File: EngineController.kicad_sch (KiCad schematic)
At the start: 37 parts, among them J1 RBUS, U1 ESP32-S3, Y1 R940000171

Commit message: Finished schematic
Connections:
- net BUCK_EN: no longer U1.43 (GPIO38)
- net CAN_RX: now also U1.6 (GPIO1/ADC1_CH0); no longer U1.39 (GPIO34)
- net CAN_TX: now also U1.7 (GPIO2/ADC1_CH1); no longer U1.38 (GPIO33)
- net Servo1PWM: now also U1.16 (GPIO11/ADC2_CH0); no longer U1.41 (GPIO36)
- net Servo2PWM: now also U1.15 (GPIO10/ADC1_CH9); no longer U1.42 (GPIO37)
- net ServoV_LOG: now also U1.17 (GPIO12/ADC2_CH1); no longer U1.40 (GPIO35)
- net GPIO5: now reaches U1.10 (GPIO5/ADC1_CH4)
- net GPIO3: now reaches U1.11 (GPIO6/ADC1_CH5)
- net GPIO1: now reaches U1.12 (GPIO7/ADC1_CH6)
- net GPIO2: now reaches U1.13 (GPIO8/ADC1_CH7)
- net GPIO0: now reaches U1.14 (GPIO9/ADC1_CH8)
- net GPIO4: now reaches U1.9 (GPIO4/ADC1_CH3)
- new net AIN0N: U1.42 (GPIO37)
- new net AIN0P: U1.43 (GPIO38)
- new net AIN1N: U1.41 (GPIO36)
- new net AIN1P: U1.40 (GPIO35)
- new net AIN2N: U1.38 (GPIO33)
- new net AIN2P: U1.39 (GPIO34)
- no-connect marks 30 -> 19
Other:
- added sheet Pyro (Pyro.kicad_sch)
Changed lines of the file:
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@@
   (no_connect (at 135.89 82.55))
   (no_connect (at 135.89 115.57))
-  (no_connect (at 69.85 95.25))
-  (no_connect (at 69.85 80.01))
-  (no_connect (at 69.85 72.39))
   (no_connect (at 135.89 80.01))
   (no_connect (at 135.89 130.81))
-  (no_connect (at 69.85 85.09))
   (no_connect (at 69.85 118.11))
   (no_connect (at 69.85 77.47))
-  (no_connect (at 69.85 82.55))
   (no_connect (at 135.89 85.09))
-  (no_connect (at 69.85 92.71))
   (no_connect (at 135.89 128.27))
   (no_connect (at 69.85 62.23))
   (no_connect (at 135.89 113.03))
-  (no_connect (at 69.85 97.79))
-  (no_connect (at 69.85 87.63))
   (no_connect (at 135.89 87.63))
   (no_connect (at 135.89 92.71))
@@
   (no_connect (at 135.89 77.47))
   (no_connect (at 135.89 123.19))
-  (no_connect (at 69.85 74.93))
   (no_connect (at 69.85 123.19))
-  (no_connect (at 69.85 90.17))
   (no_connect (at 69.85 125.73))
-  (no_connect (at 69.85 100.33))
   (no_connect (at 135.89 110.49))
   (wire (pts (xy 120.65 25.4) (xy 120.65 35.56))
@@
     (stroke (width 0) (type default))
   )
-  (wire (pts (xy 139.7 97.79) (xy 135.89 97.79))
-    (stroke (width 0) (type default))
-  )
   (wire (pts (xy 45.72 165.1) (xy 53.34 165.1))
     (stroke (width 0) (type default))
@@
     (stroke (width 0) (type default))
   )
+  (wire (pts (xy 207.264 127) (xy 214.884 127))
+    (stroke (width 0) (type default))
+  )
   (polyline (pts (xy 12.7 12.7) (xy 175.26 12.7))
     (stroke (width 0) (type default))
@@
     (stroke (width 0) (type default))
   )
+  (wire (pts (xy 205.994 123.19) (xy 214.884 123.19))
+    (stroke (width 0) (type default))
+  )
   (wire (pts (xy 58.42 21.59) (xy 58.42 26.67))
     (stroke (width 0) (type default))
@@
     (stroke (width 0) (type default))
   )
-  (wire (pts (xy 139.7 95.25) (xy 135.89 95.25))
-    (stroke (width 0) (type default))
-  )
   (wire (pts (xy 58.42 26.67) (xy 58.42 40.64))
     (stroke (width 0) (type default))
@@
   )
   (wire (pts (xy 167.64 127) (xy 167.64 132.08))
+    (stroke (width 0) (type default))
+  )
+  (wire (pts (xy 207.264 130.556) (xy 214.884 130.556))
     (stroke (width 0) (type default))
   )
@@
     (effects (font (size 1.27 1.27)) (justify right bottom))
   )
+  (label "Nuke 1" (at 207.264 127 0) (fields_autoplaced)
+    (effects (font (size 1.27 1.27)) (justify left bottom))
+  )
   (label "MOSI" (at 220.98 81.28 0) (fields_autoplaced)
     (effects (font (size 1.27 1.27)) (justify left bottom))
   )
-  (label "Servo1PWM" (at 135.89 102.87 0) (fields_autoplaced)
-    (effects (font (size 1.27 1.27)) (justify left bottom))
-  )
   (label "CHIP_PU" (at 36.83 165.1 180) (fields_autoplaced)
     (effects (font (size 1.27 1.27)) (justify right bottom))
@@
     (effects (font (size 1.27 1.27)) (justify left bottom))
   )
+  (label "AIN0P" (at 135.89 107.95 0) (fields_autoplaced)
+    (effects (font (size 1.27 1.27)) (justify left bottom))
+  )
   (label "MISO" (at 220.98 83.82 0) (fields_autoplaced)
     (effects (font (size 1.27 1.27)) (justify left bottom))
@@
     (effects (font (size 1.27 1.27)) (justify left bottom))
   )
+  (label "Servo2PWM" (at 69.85 95.25 180) (fields_autoplaced)
+    (effects (font (size 1.27 1.27)) (justify right bottom))
+  )
   (label "CAN+" (at 115.57 185.42 0) (fields_autoplaced)
     (effects (font (size 1.27 1.27)) (justify left bottom))
@@
     (effects (font (size 1.27 1.27)) (justify left bottom))
   )
+  (label "Servo1PWM" (at 69.85 97.79 180) (fields_autoplaced)
+    (effects (font (size 1.27 1.27)) (justify right bottom))
+  )
   (label "Data+" (at 99.06 160.02 0) (fields_autoplaced)
     (effects (font (size 1.27 1.27)) (justify left bottom))
@@
     (effects (font (size 1.27 1.27)) (justify left bottom))
   )
+  (label "GPIO1" (at 69.85 87.63 180) (fields_autoplaced)
+    (effects (font (size 1.27 1.27)) (justify right bottom))
+  )
   (label "MOSI" (at 66.04 105.41 180) (fields_autoplaced)
     (effects (font (size 1.27 1.27)) (justify right bottom))
   )
-  (label "CAN_TX" (at 139.7 95.25 0) (fields_autoplaced)
-    (effects (font (size 1.27 1.27)) (justify left bottom))
+  (label "GPIO0" (at 69.85 92.71 180) (fields_autoplaced)
+    (effects (font (size 1.27 1.27)) (justify right bottom))
+  )
+  (label "AIN2N" (at 135.89 95.25 0) (fields_autoplaced)
+    (effects (font (size 1.27 1.27)) (justify left bottom))
+  )
+  (label "CAN_TX" (at 69.85 74.93 180) (fields_autoplaced)
+    (effects (font (size 1.27 1.27)) (justify right bottom))
   )
   (label "SCLK" (at 144.78 72.39 0) (fields_autoplaced)
@@
     (effects (font (size 1.27 1.27)) (justify left bottom))
   )
+  (label "Cont 1" (at 207.264 130.556 0) (fields_autoplaced)
+    (effects (font (size 1.27 1.27)) (justify left bottom))
+  )
   (label "Data-" (at 99.06 162.56 0) (fields_autoplaced)
     (effects (font (size 1.27 1.27)) (justify left bottom))
@@
     (effects (font (size 1.27 1.27)) (justify left bottom))
   )
+  (label "GPIO2" (at 69.85 90.17 180) (fields_autoplaced)
+    (effects (font (size 1.27 1.27)) (justify right bottom))
+  )
+  (label "AIN2P" (at 135.89 97.79 0) (fields_autoplaced)
+    (effects (font (size 1.27 1.27)) (justify left bottom))
+  )
   (label "BOOT" (at 68.58 165.1 180) (fields_autoplaced)
     (effects (font (size 1.27 1.27)) (justify right bottom))
   )
-  (label "ServoV_LOG" (at 135.89 100.33 0) (fields_autoplaced)
-    (effects (font (size 1.27 1.27)) (justify left bottom))
-  )
-  (label "CAN_RX" (at 139.7 97.79 0) (fields_autoplaced)
+  (label "ServoV_LOG" (at 69.85 100.33 180) (fields_autoplaced)
+    (effects (font (size 1.27 1.27)) (justify right bottom))
+  )
+  (label "GPIO5" (at 69.85 82.55 180) (fields_autoplaced)
+    (effects (font (size 1.27 1.27)) (justify right bottom))
+  )
+  (label "GPIO3" (at 69.85 85.09 180) (fields_autoplaced)
+    (effects (font (size 1.27 1.27)) (justify right bottom))
+  )
+  (label "CAN_RX" (at 69.85 72.39 180) (fields_autoplaced)
+    (effects (font (size 1.27 1.27)) (justify right bottom))
+  )
+  (label "AIN1P" (at 135.89 100.33 0) (fields_autoplaced)
     (effects (font (size 1.27 1.27)) (justify left bottom))
   )
@@
     (effects (font (size 1.27 1.27)) (justify right bottom))
   )
-  (label "BUCK_EN" (at 135.89 107.95 0) (fields_autoplaced)
+  (label "AIN1N" (at 135.89 102.87 0) (fields_autoplaced)
     (effects (font (size 1.27 1.27)) (justify left bottom))
   )
@@
     (effects (font (size 1.27 1.27)) (justify left bottom))
   )
-  (label "Servo2PWM" (at 135.89 105.41 0) (fields_autoplaced)
+  (label "PyroPWR" (at 205.994 123.19 0) (fields_autoplaced)
+    (effects (font (size 1.27 1.27)) (justify left bottom))
+  )
+  (label "AIN0N" (at 135.89 105.41 0) (fields_autoplaced)
     (effects (font (size 1.27 1.27)) (justify left bottom))
   )
@@
   (label "CAN-" (at 115.57 187.96 0) (fields_autoplaced)
     (effects (font (size 1.27 1.27)) (justify left bottom))
+  )
+  (label "GPIO4" (at 69.85 80.01 180) (fields_autoplaced)
+    (effects (font (size 1.27 1.27)) (justify right bottom))
   )
   (label "BuckPGOOD" (at 218.44 33.02 0) (fields_autoplaced)
@@
       (effects (font (size 1.27 1.27)) (justify right) hide)
     )
+  )
+  (hierarchical_label "PyroPWR" (shape output) (at 214.884 123.19 0) (fields_autoplaced)
+    (effects (font (size 1.27 1.27)) (justify left))
+  )
+  (hierarchical_label "Cont 1" (shape input) (at 214.884 130.556 0) (fields_autoplaced)
+    (effects (font (size 1.27 1.27)) (justify left))
+  )
+  (hierarchical_label "Nuke 1" (shape output) (at 214.884 127 0) (fields_autoplaced)
+    (effects (font (size 1.27 1.27)) (justify left))
   )
   (symbol (lib_id "power:+3.3V") (at 30.48 182.88 0) (unit 1)
@@
       )
     )
+  )
+  (sheet (at 214.884 121.412) (size 12.7 14.732) (fields_autoplaced)
+    (stroke (width 0.1524) (type solid))
+    (fill (color 0 0 0 0.0000))
+    (property "Sheetname" "Pyro" (at 214.884 120.7004 0)
+      (effects (font (size 1.27 1.27)) (justify left bottom))
+    )
+    (property "Sheetfile" "Pyro.kicad_sch" (at 214.884 136.7286 0)
+      (effects (font (size 1.27 1.27)) (justify left top))
+    )
+    (instances
+      (project "EngineController"
+        (path "/7db990e4-92e1-4f99-b4d2-435bbec1ba83" (page "9"))
+      )
+    )

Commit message: Forgot Pyro
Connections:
- net Cont 1: now also U1.31 (SPIWP/GPIO28)
- net Nuke 1: now also U1.30 (SPIHD/GPIO27)
- no-connect marks 19 -> 17
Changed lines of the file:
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@@
   )
   (no_connect (at 135.89 90.17))
-  (no_connect (at 135.89 82.55))
   (no_connect (at 135.89 115.57))
-  (no_connect (at 135.89 80.01))
   (no_connect (at 135.89 130.81))
   (no_connect (at 69.85 118.11))
@@
     (stroke (width 0) (type default))
   )
-  (polyline (pts (xy 137.16 76.2) (xy 137.16 93.98))
-    (stroke (width 0) (type default))
-  )
   (wire (pts (xy 29.21 135.89) (xy 34.29 135.89))
     (stroke (width 0) (type default))
@@
     (stroke (width 0) (type default))
   )
-  (polyline (pts (xy 137.16 93.98) (xy 116.84 93.98))
-    (stroke (width 0) (type default))
-  )
   (wire (pts (xy 156.21 127) (xy 156.21 128.27))
     (stroke (width 0) (type default))
@@
     (stroke (width 0) (type default))
   )
-  (polyline (pts (xy 116.84 76.2) (xy 116.84 93.98))
-    (stroke (width 0) (type default))
-  )
   (wire (pts (xy 278.13 33.02) (xy 273.05 33.02))
     (stroke (width 0) (type default))
@@
   )
   (wire (pts (xy 20.32 135.89) (xy 29.21 135.89))
-    (stroke (width 0) (type default))
-  )
-  (polyline (pts (xy 137.16 76.2) (xy 116.84 76.2))
     (stroke (width 0) (type default))
   )
@@
     (effects (font (size 1.27 1.27)) (justify left bottom))
   )
+  (label "Cont 1" (at 135.89 82.55 0) (fields_autoplaced)
+    (effects (font (size 1.27 1.27)) (justify left bottom))
+  )
   (label "BOOT" (at 68.58 165.1 180) (fields_autoplaced)
     (effects (font (size 1.27 1.27)) (justify right bottom))
@@
     (effects (font (size 1.27 1.27)) (justify left bottom))
   )
+  (label "Nuke 1" (at 135.89 80.01 0) (fields_autoplaced)
+    (effects (font (size 1.27 1.27)) (justify left bottom))
+  )

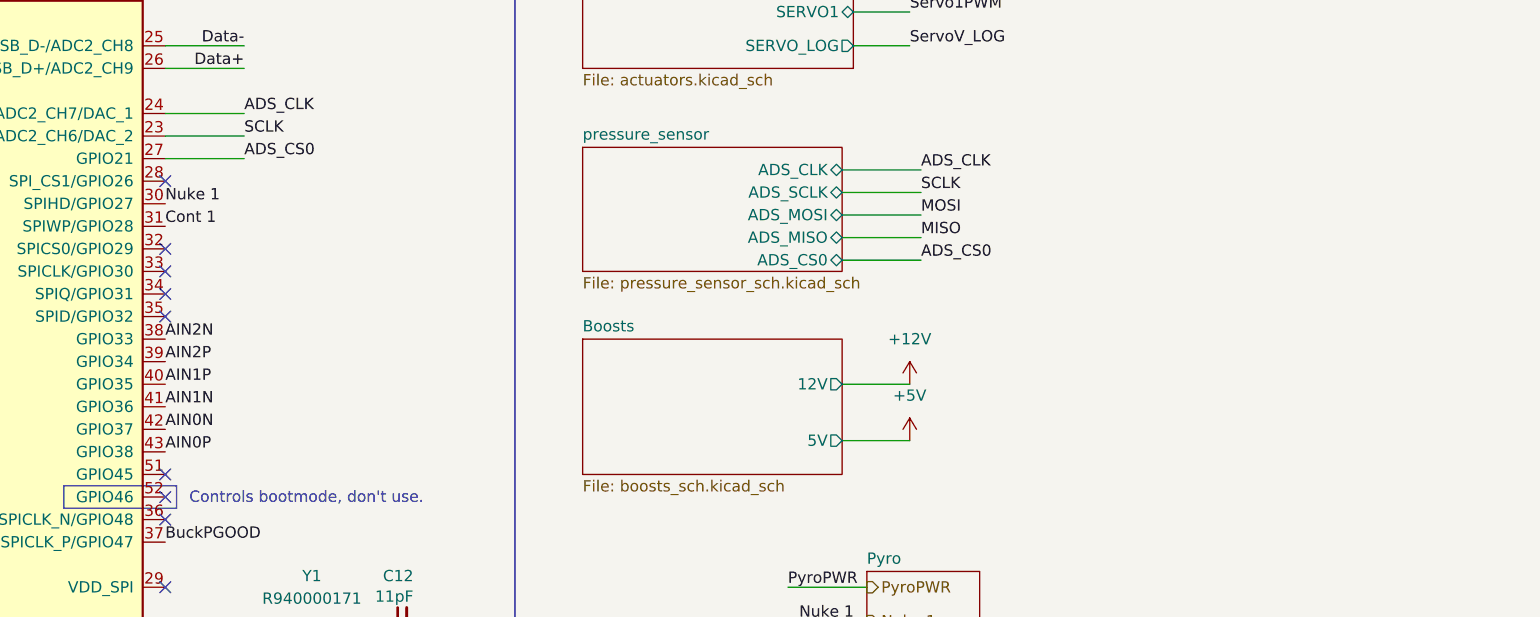
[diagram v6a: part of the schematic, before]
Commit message: forgot sd card and added ads chip
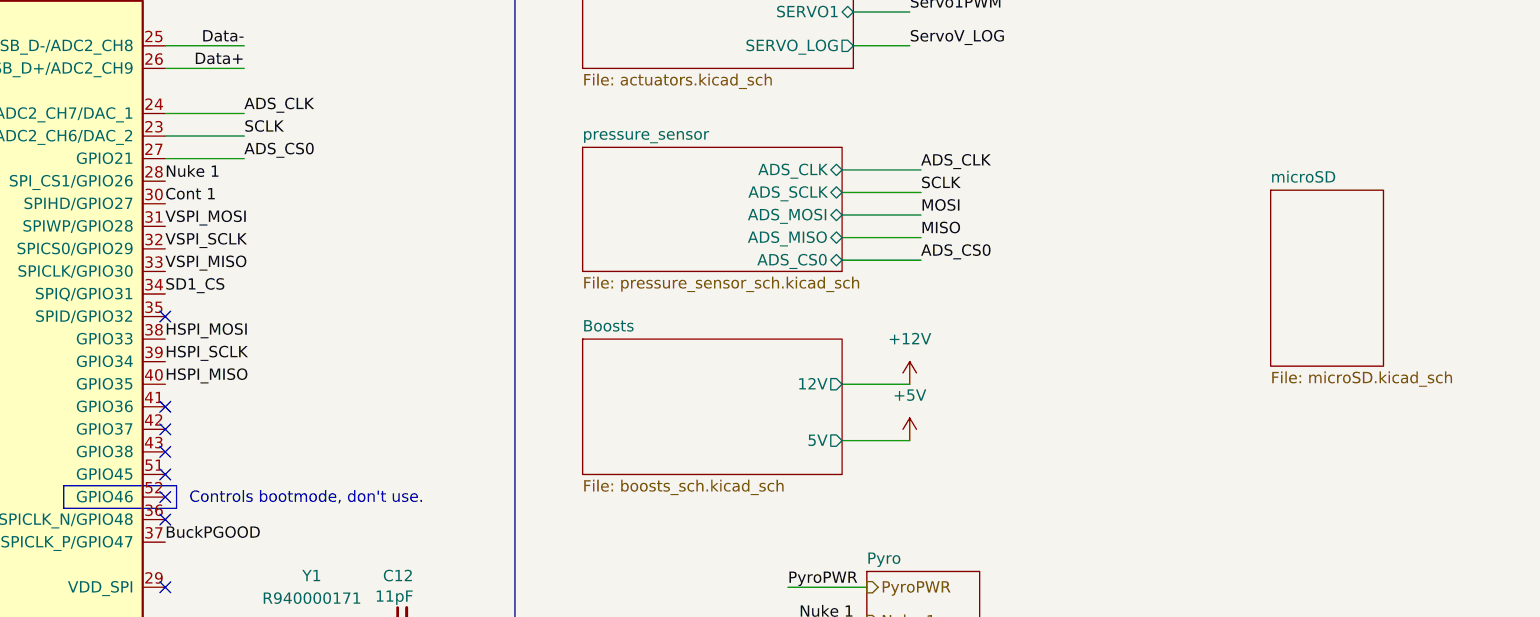
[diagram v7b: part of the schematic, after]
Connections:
- net Cont 1: now also U1.30 (SPIHD/GPIO27); no longer U1.31 (SPIWP/GPIO28)
- net Nuke 1: now also U1.28 (SPI_CS1/GPIO26); no longer U1.30 (SPIHD/GPIO27)
- net VSPI_SCLK: now reaches U1.32 (SPICS0/GPIO29)
- net VSPI_MISO: now reaches U1.33 (SPICLK/GPIO30)
- net SD1_CS: now reaches U1.34 (SPIQ/GPIO31)
- net AIN0N: no longer names the net of U1.42 (GPIO37)
- net AIN0P: no longer names the net of U1.43 (GPIO38)
- net AIN1N: no longer names the net of U1.41 (GPIO36)
- net AIN1P renamed HSPI_MISO
- net AIN2N renamed HSPI_MOSI
- net AIN2P renamed HSPI_SCLK
- new net VSPI_MOSI: U1.31 (SPIWP/GPIO28)
- no-connect marks 17 -> 16
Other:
- added sheet microSD (microSD.kicad_sch)
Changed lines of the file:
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@@
   (junction (at 135.89 143.51) (diameter 0) (color 0 0 0 0)
   )
-  (no_connect (at 135.89 90.17))
   (no_connect (at 135.89 115.57))
+  (no_connect (at 135.89 105.41))
+  (no_connect (at 135.89 107.95))
   (no_connect (at 135.89 130.81))
   (no_connect (at 69.85 118.11))
   (no_connect (at 69.85 77.47))
-  (no_connect (at 135.89 85.09))
+  (no_connect (at 135.89 102.87))
   (no_connect (at 135.89 128.27))
   (no_connect (at 69.85 62.23))
   (no_connect (at 135.89 113.03))
-  (no_connect (at 135.89 87.63))
   (no_connect (at 135.89 92.71))
   (no_connect (at 69.85 120.65))
-  (no_connect (at 135.89 77.47))
   (no_connect (at 135.89 123.19))
   (no_connect (at 69.85 123.19))
@@
     (effects (font (size 1.27 1.27)) (justify left bottom))
   )
-  (label "AIN0P" (at 135.89 107.95 0) (fields_autoplaced)
-    (effects (font (size 1.27 1.27)) (justify left bottom))
-  )
   (label "MISO" (at 220.98 83.82 0) (fields_autoplaced)
     (effects (font (size 1.27 1.27)) (justify left bottom))
@@
     (effects (font (size 1.27 1.27)) (justify right bottom))
   )
+  (label "VSPI_SCLK" (at 135.89 85.09 0) (fields_autoplaced)
+    (effects (font (size 1.27 1.27)) (justify left bottom))
+  )
+  (label "SD1_CS" (at 135.89 90.17 0) (fields_autoplaced)
+    (effects (font (size 1.27 1.27)) (justify left bottom))
+  )
   (label "MOSI" (at 66.04 105.41 180) (fields_autoplaced)
     (effects (font (size 1.27 1.27)) (justify right bottom))
@@
     (effects (font (size 1.27 1.27)) (justify right bottom))
   )
-  (label "AIN2N" (at 135.89 95.25 0) (fields_autoplaced)
+  (label "HSPI_SCLK" (at 135.89 97.79 0) (fields_autoplaced)
     (effects (font (size 1.27 1.27)) (justify left bottom))
   )
@@
     (effects (font (size 1.27 1.27)) (justify left bottom))
   )
+  (label "VSPI_MISO" (at 135.89 87.63 0) (fields_autoplaced)
+    (effects (font (size 1.27 1.27)) (justify left bottom))
+  )
   (label "BOOT" (at 53.34 191.77 180) (fields_autoplaced)
     (effects (font (size 1.27 1.27)) (justify right bottom))
@@
     (effects (font (size 1.27 1.27)) (justify right bottom))
   )
-  (label "AIN2P" (at 135.89 97.79 0) (fields_autoplaced)
-    (effects (font (size 1.27 1.27)) (justify left bottom))
-  )
-  (label "Cont 1" (at 135.89 82.55 0) (fields_autoplaced)
+  (label "Cont 1" (at 135.89 80.01 0) (fields_autoplaced)
     (effects (font (size 1.27 1.27)) (justify left bottom))
   )
@@
     (effects (font (size 1.27 1.27)) (justify right bottom))
   )
-  (label "AIN1P" (at 135.89 100.33 0) (fields_autoplaced)
-    (effects (font (size 1.27 1.27)) (justify left bottom))
-  )
   (label "BUCK_EN" (at 226.06 21.59 180) (fields_autoplaced)
     (effects (font (size 1.27 1.27)) (justify right bottom))
   )
-  (label "AIN1N" (at 135.89 102.87 0) (fields_autoplaced)
-    (effects (font (size 1.27 1.27)) (justify left bottom))
-  )
   (label "RXD" (at 64.77 115.57 180) (fields_autoplaced)
     (effects (font (size 1.27 1.27)) (justify right bottom))
@@
     (effects (font (size 1.27 1.27)) (justify left bottom))
   )
-  (label "Nuke 1" (at 135.89 80.01 0) (fields_autoplaced)
+  (label "Nuke 1" (at 135.89 77.47 0) (fields_autoplaced)
     (effects (font (size 1.27 1.27)) (justify left bottom))
   )
@@
     (effects (font (size 1.27 1.27)) (justify left bottom))
   )
-  (label "AIN0N" (at 135.89 105.41 0) (fields_autoplaced)
-    (effects (font (size 1.27 1.27)) (justify left bottom))
-  )
   (label "CAN_RX" (at 115.57 182.88 0) (fields_autoplaced)
     (effects (font (size 1.27 1.27)) (justify left bottom))
   )
+  (label "VSPI_MOSI" (at 135.89 82.55 0) (fields_autoplaced)
+    (effects (font (size 1.27 1.27)) (justify left bottom))
+  )
   (label "Data+" (at 144.78 64.77 180) (fields_autoplaced)
     (effects (font (size 1.27 1.27)) (justify right bottom))
@@
     (effects (font (size 1.27 1.27)) (justify left bottom))
   )
+  (label "HSPI_MISO" (at 135.89 100.33 0) (fields_autoplaced)
+    (effects (font (size 1.27 1.27)) (justify left bottom))
+  )
   (label "TXD" (at 17.78 21.59 0) (fields_autoplaced)
     (effects (font (size 1.27 1.27)) (justify left bottom))
@@
   (label "CHIP_PU" (at 39.37 191.77 180) (fields_autoplaced)
     (effects (font (size 1.27 1.27)) (justify right bottom))
+  )
+  (label "HSPI_MOSI" (at 135.89 95.25 0) (fields_autoplaced)
+    (effects (font (size 1.27 1.27)) (justify left bottom))
   )
   (global_label "RBUS_uC_V" (shape input) (at 123.19 25.4 270) (fields_autoplaced)
@@
       )
     )
+  )
+  (sheet (at 260.35 78.486) (size 12.7 19.812) (fields_autoplaced)
+    (stroke (width 0.1524) (type solid))
+    (fill (color 0 0 0 0.0000))
+    (property "Sheetname" "microSD" (at 260.35 77.7744 0)
+      (effects (font (size 1.27 1.27)) (justify left bottom))
+    )
+    (property "Sheetfile" "microSD.kicad_sch" (at 260.35 98.8826 0)
+      (effects (font (size 1.27 1.27)) (justify left top))
+    )
+    (instances
+      (project "EngineController"
+        (path "/7db990e4-92e1-4f99-b4d2-435bbec1ba83" (page "10"))
+      )
+    )

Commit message: update
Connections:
- net BUCK_EN: now also U1.18 (GPIO13/ADC2_CH2)
- net MISO: no longer U1.18 (GPIO13/ADC2_CH2)
- net MOSI: no longer U1.19 (GPIO14/ADC2_CH3)
- no-connect marks 16 -> 17
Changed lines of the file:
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@@
   (junction (at 135.89 143.51) (diameter 0) (color 0 0 0 0)
   )
+  (no_connect (at 69.85 105.41))
   (no_connect (at 135.89 115.57))
   (no_connect (at 135.89 105.41))
@@
     (stroke (width 0) (type default))
   )
-  (wire (pts (xy 66.04 105.41) (xy 69.85 105.41))
-    (stroke (width 0) (type default))
-  )
   (wire (pts (xy 160.02 127) (xy 156.21 127))
     (stroke (width 0) (type default))
@@
   )
   (wire (pts (xy 20.32 140.97) (xy 29.21 140.97))
-    (stroke (width 0) (type default))
-  )
-  (wire (pts (xy 66.04 102.87) (xy 69.85 102.87))
     (stroke (width 0) (type default))
   )
@@
     (effects (font (size 1.27 1.27)) (justify left bottom))
   )
-  (label "MOSI" (at 66.04 105.41 180) (fields_autoplaced)
-    (effects (font (size 1.27 1.27)) (justify right bottom))
-  )
   (label "GPIO0" (at 69.85 92.71 180) (fields_autoplaced)
     (effects (font (size 1.27 1.27)) (justify right bottom))
@@
     (effects (font (size 1.27 1.27)) (justify left bottom))
   )
-  (label "MISO" (at 66.04 102.87 180) (fields_autoplaced)
-    (effects (font (size 1.27 1.27)) (justify right bottom))
-  )
   (label "TXD" (at 29.21 38.1 0) (fields_autoplaced)
     (effects (font (size 1.27 1.27)) (justify left bottom))
@@
     (effects (font (size 1.27 1.27)) (justify left bottom))
   )
+  (label "BUCK_EN" (at 69.85 102.87 180) (fields_autoplaced)
+    (effects (font (size 1.27 1.27)) (justify right bottom))
+  )
   (label "CAN_RX" (at 115.57 182.88 0) (fields_autoplaced)
